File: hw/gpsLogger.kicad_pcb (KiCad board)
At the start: 2 copper layers, 42 x 72.8 mm, 0 parts

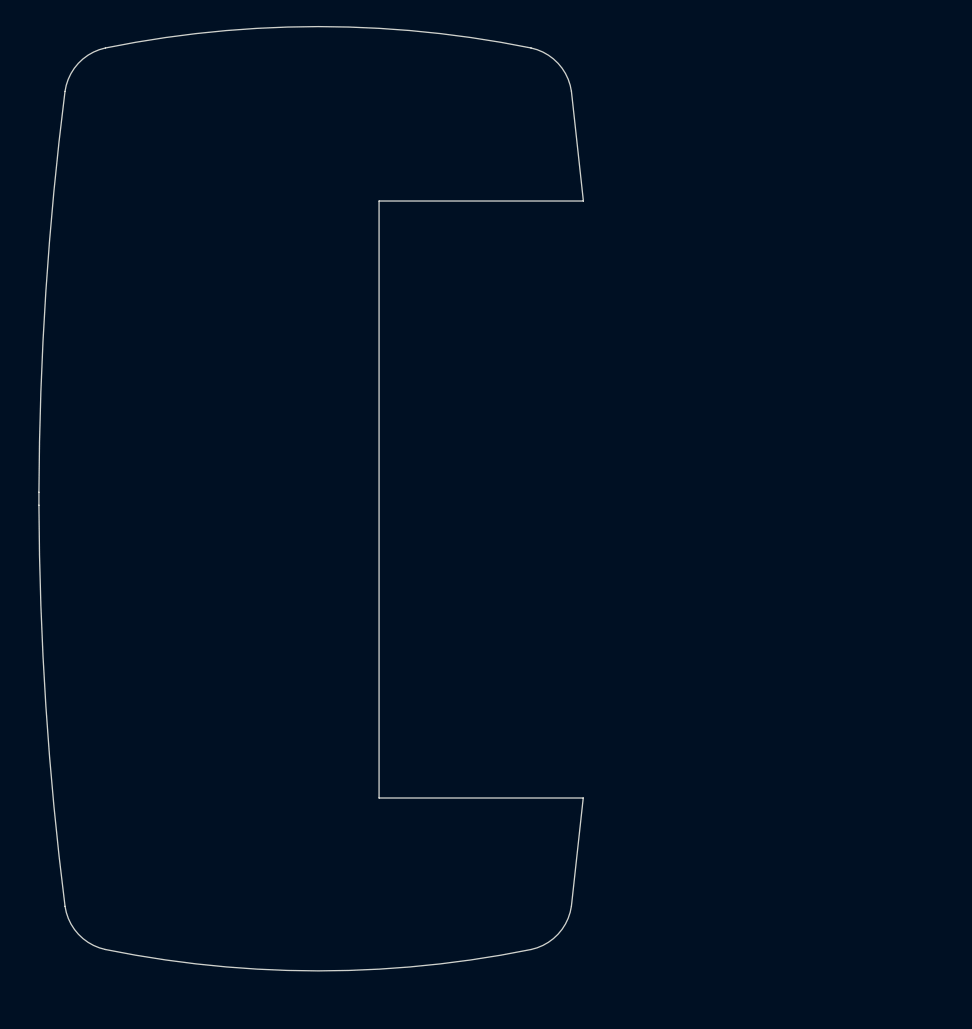
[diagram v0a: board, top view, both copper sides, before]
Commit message: Added USB vertical footprint. uSD card footprint. Did schematic, started rough PCB
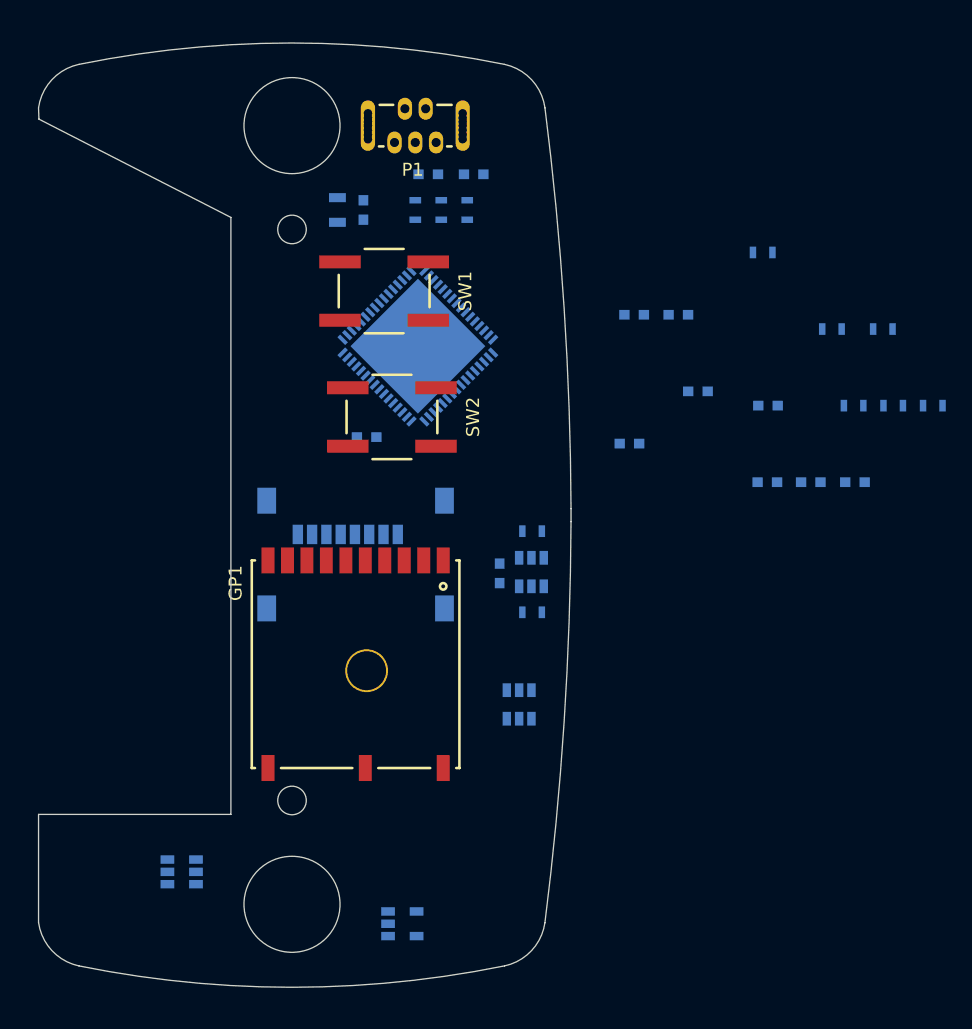
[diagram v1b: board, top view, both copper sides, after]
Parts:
- added C1: C, Capacitors_SMD:C_0603, B.Cu at (147.0, 78.0)
- added C10: C, Capacitors_SMD:C_0603, B.Cu at (172.8, 92.0)
- added C11: C, Capacitors_SMD:C_0603, B.Cu at (178.2, 93.1)
- added C12: C, Capacitors_SMD:C_0603, B.Cu at (171.3, 86.1)
- added C13: C, Capacitors_SMD:C_0603, B.Cu at (184.9, 99.0)
- added C2: C, Capacitors_SMD:C_0603, B.Cu at (155.5, 75.2)
- added C3: C, Capacitors_SMD:C_0603, B.Cu at (152.0, 75.2)
- added C4: C, Capacitors_SMD:C_0603, B.Cu at (147.2, 95.5)
- added C5: C, Capacitors_SMD:C_0603, B.Cu at (157.5, 106.0)
- added C6: C, Capacitors_SMD:C_0603, B.Cu at (178.1, 99.0)
- added C7: C, Capacitors_SMD:C_0603, B.Cu at (167.5, 96.0)
- added C8: C, Capacitors_SMD:C_0603, B.Cu at (167.9, 86.1)
- added C9: C, Capacitors_SMD:C_0603, B.Cu at (181.5, 99.0)
- added FB1: FILTER, Resistors_SMD:R_0805, B.Cu at (145.0, 78.0)
- added GP1: GPS, footprints:PA6C, F.Cu at (147.2, 113.0)
- added IC1: MSP430F55xx, Housings_DFN_QFN:QFN-64-1EP_9x9mm_Pitch0.5mm, B.Cu at (151.2, 88.5)
- added P1: USB_OTG, footprints:USB_VERT, F.Cu at (151.0, 71.5)
- added R1: R, Resistors_SMD:R_0603, B.Cu at (155.0, 78.0)
- added R10: R, Resistors_SMD:R_0603, B.Cu at (177.8, 81.3)
- added R11: 1K, Resistors_SMD:R_0603, B.Cu at (187.0, 87.2)
- added R2: R, Resistors_SMD:R_0603, B.Cu at (153.0, 78.0)
- added R3: R, Resistors_SMD:R_0603, B.Cu at (151.0, 78.0)
- added R4: R, Resistors_SMD:R_0603, B.Cu at (184.8, 93.1)
- added R5: R, Resistors_SMD:R_0603, B.Cu at (160.0, 102.8)
- added R6: R, Resistors_SMD:R_0603, B.Cu at (160.0, 109.0)
- added R7: R, Resistors_SMD:R_0603, B.Cu at (187.8, 93.1)
- added R8: R, Resistors_SMD:R_0603, B.Cu at (190.9, 93.1)
- added R9: 330R, Resistors_SMD:R_0603, B.Cu at (183.1, 87.2)
- added REF**: SolderWirePad_single_2mmDrill, Wire_Pads:SolderWirePad_single_2mmDrill, F.Cu at (141.5, 123.5)
- added REF**: SolderWirePad_single_2mmDrill, Wire_Pads:SolderWirePad_single_2mmDrill, F.Cu at (141.5, 79.5)
- added REF**: SolderWirePad_single_2mmDrill, Wire_Pads:SolderWirePad_single_2mmDrill, F.Cu at (141.5, 131.5)
- added REF**: SolderWirePad_single_2mmDrill, Wire_Pads:SolderWirePad_single_2mmDrill, F.Cu at (141.5, 71.5)
- added SW1: SW_PUSH, cameraTrigger_rev1_0:EVQ_switch, F.Cu at (148.6, 84.2)
- added SW2: SW_PUSH, cameraTrigger_rev1_0:EVQ_switch, F.Cu at (149.2, 94.0)
- added U1: TPS27081A, TO_SOT_Packages_SMD:SOT-23-6, B.Cu at (159.9, 105.9)
- added U2: MCP73812, TO_SOT_Packages_SMD:SOT-23-5, B.Cu at (150.0, 133.0)
- added U3: uSD, footprints:SD_holder_472190001, B.Cu at (145.7, 103.0)
- added U4: TPS27081A, TO_SOT_Packages_SMD:SOT-23-6, B.Cu at (159.0, 116.1)
- added U5: S8261, TO_SOT_Packages_SMD:SOT-23-6, B.Cu at (133.0, 129.0)
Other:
- board size 42 x 72.8 mm -> 41 x 72.8 mm

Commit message: Added LED footprint, and Beagle GPS logo. Schematic done, PCB done.
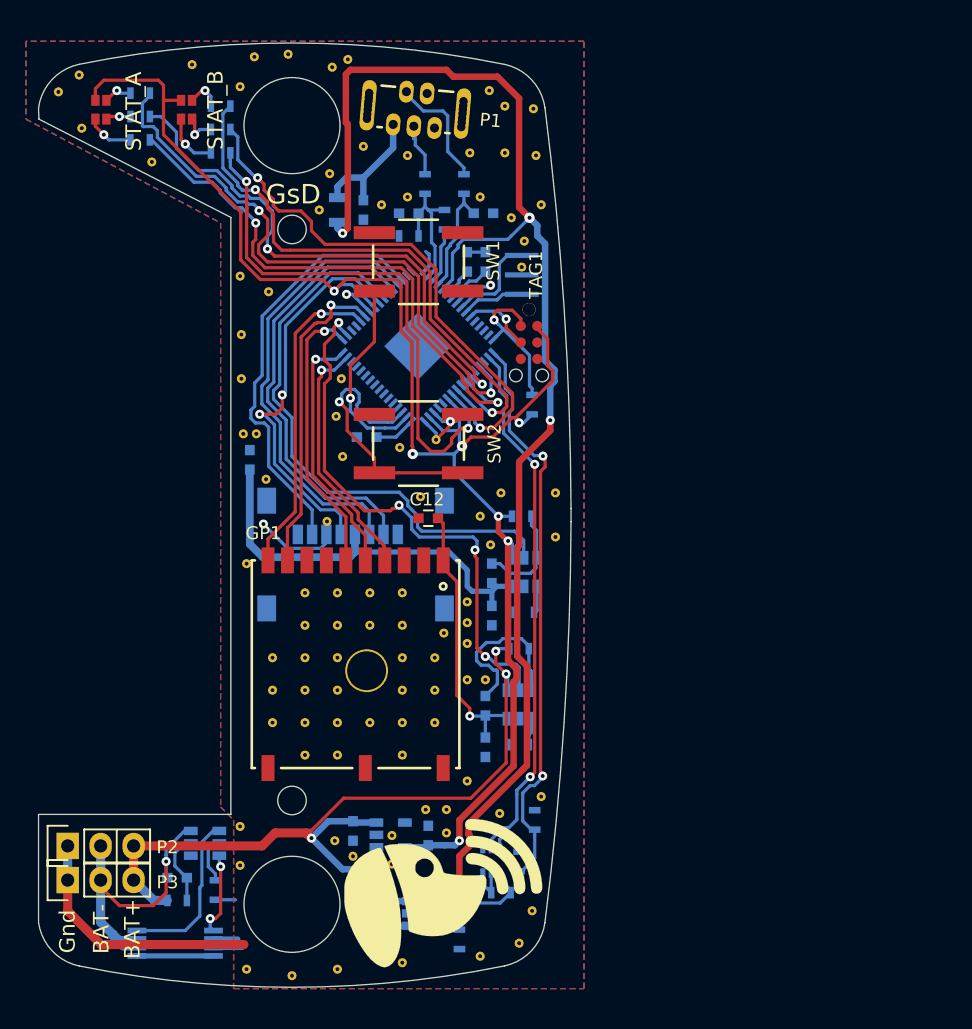
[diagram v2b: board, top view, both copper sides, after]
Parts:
- added C14: C, Capacitors_SMD:C_0603, B.Cu at (146.2, 125.8)
- added C15: C, Capacitors_SMD:C_0603, B.Cu at (152.0, 126.2)
- added C16: C, Capacitors_SMD:C_0603, B.Cu at (156.4, 82.0)
- added C17: C, Capacitors_SMD:C_0603, B.Cu at (155.0, 82.0)
- added D1: Led_RGB_CA, footprints:LITEON_RGB, F.Cu at (126.8, 70.3)
- added D2: Led_RGB_CA, footprints:LITEON_RGB, F.Cu at (133.4, 70.3)
- added G***: LOGO, LOGO, F.Cu at (152.8, 130.8)
- added P2: CONN_01X03, Socket_Strips:Socket_Strip_Straight_1x03, F.Cu at (124.2, 127.0)
- added P3: CONN_01X03, Socket_Strips:Socket_Strip_Straight_1x03, F.Cu at (124.2, 129.6)
- added Q1: Q_NMOS_AO8810, Housings_SSOP:TSSOP-8_4.4x3mm_Pitch0.65mm, B.Cu at (132.5, 134.5)
- added Q2: FG6943010R, TO_SOT_Packages_SMD:SC-70-6, B.Cu at (156.9, 128.1)
- added R12: R, Resistors_SMD:R_0603, B.Cu at (157.6, 130.6)
- added R13: R, Resistors_SMD:R_0603, B.Cu at (159.0, 128.2)
- added R14: R, Resistors_SMD:R_0603, B.Cu at (160.2, 125.0)
- added R15: R, Resistors_SMD:R_0603, B.Cu at (160.0, 93.0)
- added R16: R, Resistors_SMD:R_0603, B.Cu at (129.8, 69.0)
- added R17: R, Resistors_SMD:R_0603, B.Cu at (129.8, 70.8)
- added R18: R, Resistors_SMD:R_0603, B.Cu at (129.8, 72.6)
- added R19: R, Resistors_SMD:R_0603, B.Cu at (136.0, 70.0)
- added R20: R, Resistors_SMD:R_0603, B.Cu at (136.0, 71.8)
- added R21: R, Resistors_SMD:R_0603, B.Cu at (136.0, 73.6)
- added REF**: SolderWirePad_single_2mmDrill, Wire_Pads:SolderWirePad_single_2mmDrill, F.Cu at (160.7, 123.2)
- added REF**: SolderWirePad_single_2mmDrill, Wire_Pads:SolderWirePad_single_2mmDrill, F.Cu at (160.7, 77.6)
- added REF**: SolderWirePad_single_2mmDrill, Wire_Pads:SolderWirePad_single_2mmDrill, F.Cu at (160.1, 70.2)
- added REF**: SolderWirePad_single_2mmDrill, Wire_Pads:SolderWirePad_single_2mmDrill, F.Cu at (160.3, 73.8)
- added REF**: SolderWirePad_single_2mmDrill, Wire_Pads:SolderWirePad_single_2mmDrill, F.Cu at (157.9, 73.6)
- added REF**: SolderWirePad_single_2mmDrill, Wire_Pads:SolderWirePad_single_2mmDrill, F.Cu at (157.9, 70.0)
- added REF**: SolderWirePad_single_2mmDrill, Wire_Pads:SolderWirePad_single_2mmDrill, F.Cu at (156.7, 68.8)
- added REF**: SolderWirePad_single_2mmDrill, Wire_Pads:SolderWirePad_single_2mmDrill, F.Cu at (137.6, 87.6)
- added REF**: SolderWirePad_single_2mmDrill, Wire_Pads:SolderWirePad_single_2mmDrill, F.Cu at (137.6, 91.0)
- added REF**: SolderWirePad_single_2mmDrill, Wire_Pads:SolderWirePad_single_2mmDrill, F.Cu at (137.5, 83.1)
- added REF**: SolderWirePad_single_2mmDrill, Wire_Pads:SolderWirePad_single_2mmDrill, F.Cu at (139.7, 84.3)
- added REF**: SolderWirePad_single_2mmDrill, Wire_Pads:SolderWirePad_single_2mmDrill, F.Cu at (137.5, 68.5)
- added REF**: SolderWirePad_single_2mmDrill, Wire_Pads:SolderWirePad_single_2mmDrill, F.Cu at (145.3, 91.0)
- added REF**: SolderWirePad_single_2mmDrill, Wire_Pads:SolderWirePad_single_2mmDrill, F.Cu at (144.9, 93.9)
- added REF**: SolderWirePad_single_2mmDrill, Wire_Pads:SolderWirePad_single_2mmDrill, F.Cu at (145.4, 97.0)
- added REF**: SolderWirePad_single_2mmDrill, Wire_Pads:SolderWirePad_single_2mmDrill, F.Cu at (149.8, 96.3)
- added REF**: SolderWirePad_single_2mmDrill, Wire_Pads:SolderWirePad_single_2mmDrill, F.Cu at (152.6, 95.7)
- added REF**: SolderWirePad_single_2mmDrill, Wire_Pads:SolderWirePad_single_2mmDrill, F.Cu at (157.5, 124.5)
- added REF**: SolderWirePad_single_2mmDrill, Wire_Pads:SolderWirePad_single_2mmDrill, F.Cu at (155.0, 122.0)
- added REF**: SolderWirePad_single_2mmDrill, Wire_Pads:SolderWirePad_single_2mmDrill, F.Cu at (137.5, 125.5)
- added REF**: SolderWirePad_single_2mmDrill, Wire_Pads:SolderWirePad_single_2mmDrill, F.Cu at (137.5, 128.5)
- added REF**: SolderWirePad_single_2mmDrill, Wire_Pads:SolderWirePad_single_2mmDrill, F.Cu at (160.0, 132.0)
- added REF**: SolderWirePad_single_2mmDrill, Wire_Pads:SolderWirePad_single_2mmDrill, F.Cu at (130.7, 74.3)
- added REF**: SolderWirePad_single_2mmDrill, Wire_Pads:SolderWirePad_single_2mmDrill, F.Cu at (159.0, 134.5)
- added REF**: SolderWirePad_single_2mmDrill, Wire_Pads:SolderWirePad_single_2mmDrill, F.Cu at (156.0, 135.5)
- added REF**: SolderWirePad_single_2mmDrill, Wire_Pads:SolderWirePad_single_2mmDrill, F.Cu at (150.0, 136.0)
- added REF**: SolderWirePad_single_2mmDrill, Wire_Pads:SolderWirePad_single_2mmDrill, F.Cu at (145.0, 136.5)
- added REF**: SolderWirePad_single_2mmDrill, Wire_Pads:SolderWirePad_single_2mmDrill, F.Cu at (141.5, 137.0)
- added REF**: SolderWirePad_single_2mmDrill, Wire_Pads:SolderWirePad_single_2mmDrill, F.Cu at (138.0, 136.5)
- added REF**: SolderWirePad_single_2mmDrill, Wire_Pads:SolderWirePad_single_2mmDrill, F.Cu at (150.0, 107.5)
- added REF**: SolderWirePad_single_2mmDrill, Wire_Pads:SolderWirePad_single_2mmDrill, F.Cu at (152.5, 115.0)
- added REF**: SolderWirePad_single_2mmDrill, Wire_Pads:SolderWirePad_single_2mmDrill, F.Cu at (152.5, 112.5)
- added REF**: SolderWirePad_single_2mmDrill, Wire_Pads:SolderWirePad_single_2mmDrill, F.Cu at (145.0, 112.5)
- added REF**: SolderWirePad_single_2mmDrill, Wire_Pads:SolderWirePad_single_2mmDrill, F.Cu at (125.3, 71.7)
- added REF**: SolderWirePad_single_2mmDrill, Wire_Pads:SolderWirePad_single_2mmDrill, F.Cu at (142.5, 112.5)
- added REF**: SolderWirePad_single_2mmDrill, Wire_Pads:SolderWirePad_single_2mmDrill, F.Cu at (140.0, 112.5)
- added REF**: SolderWirePad_single_2mmDrill, Wire_Pads:SolderWirePad_single_2mmDrill, F.Cu at (142.5, 110.0)
- added REF**: SolderWirePad_single_2mmDrill, Wire_Pads:SolderWirePad_single_2mmDrill, F.Cu at (145.0, 110.0)
- added REF**: SolderWirePad_single_2mmDrill, Wire_Pads:SolderWirePad_single_2mmDrill, F.Cu at (147.5, 110.0)
- added REF**: SolderWirePad_single_2mmDrill, Wire_Pads:SolderWirePad_single_2mmDrill, F.Cu at (150.0, 110.0)
- added REF**: SolderWirePad_single_2mmDrill, Wire_Pads:SolderWirePad_single_2mmDrill, F.Cu at (150.0, 112.5)
- added REF**: SolderWirePad_single_2mmDrill, Wire_Pads:SolderWirePad_single_2mmDrill, F.Cu at (150.0, 115.0)
- added REF**: SolderWirePad_single_2mmDrill, Wire_Pads:SolderWirePad_single_2mmDrill, F.Cu at (145.0, 115.0)
- added REF**: SolderWirePad_single_2mmDrill, Wire_Pads:SolderWirePad_single_2mmDrill, F.Cu at (142.5, 115.0)
- added REF**: SolderWirePad_single_2mmDrill, Wire_Pads:SolderWirePad_single_2mmDrill, F.Cu at (123.5, 68.9)
- added REF**: SolderWirePad_single_2mmDrill, Wire_Pads:SolderWirePad_single_2mmDrill, F.Cu at (152.5, 117.5)
- added REF**: SolderWirePad_single_2mmDrill, Wire_Pads:SolderWirePad_single_2mmDrill, F.Cu at (150.0, 117.5)
- added REF**: SolderWirePad_single_2mmDrill, Wire_Pads:SolderWirePad_single_2mmDrill, F.Cu at (147.5, 117.5)
- added REF**: SolderWirePad_single_2mmDrill, Wire_Pads:SolderWirePad_single_2mmDrill, F.Cu at (145.0, 117.5)
- added REF**: SolderWirePad_single_2mmDrill, Wire_Pads:SolderWirePad_single_2mmDrill, F.Cu at (142.5, 117.5)
- added REF**: SolderWirePad_single_2mmDrill, Wire_Pads:SolderWirePad_single_2mmDrill, F.Cu at (145.0, 120.0)
- added REF**: SolderWirePad_single_2mmDrill, Wire_Pads:SolderWirePad_single_2mmDrill, F.Cu at (142.5, 120.0)
- added REF**: SolderWirePad_single_2mmDrill, Wire_Pads:SolderWirePad_single_2mmDrill, F.Cu at (138.6, 66.2)
- added REF**: SolderWirePad_single_2mmDrill, Wire_Pads:SolderWirePad_single_2mmDrill, F.Cu at (141.2, 66.0)
- added REF**: SolderWirePad_single_2mmDrill, Wire_Pads:SolderWirePad_single_2mmDrill, F.Cu at (145.8, 66.4)
- added REF**: SolderWirePad_single_2mmDrill, Wire_Pads:SolderWirePad_single_2mmDrill, F.Cu at (125.1, 67.6)
- added REF**: SolderWirePad_single_2mmDrill, Wire_Pads:SolderWirePad_single_2mmDrill, F.Cu at (144.6, 67.0)
- added REF**: SolderWirePad_single_2mmDrill, Wire_Pads:SolderWirePad_single_2mmDrill, F.Cu at (144.4, 75.2)
- added REF**: SolderWirePad_single_2mmDrill, Wire_Pads:SolderWirePad_single_2mmDrill, F.Cu at (143.6, 78.0)
- added REF**: SolderWirePad_single_2mmDrill, Wire_Pads:SolderWirePad_single_2mmDrill, F.Cu at (155.2, 73.6)
- added REF**: SolderWirePad_single_2mmDrill, Wire_Pads:SolderWirePad_single_2mmDrill, F.Cu at (150.4, 73.8)
- added REF**: SolderWirePad_single_2mmDrill, Wire_Pads:SolderWirePad_single_2mmDrill, F.Cu at (150.4, 77.0)
- added REF**: SolderWirePad_single_2mmDrill, Wire_Pads:SolderWirePad_single_2mmDrill, F.Cu at (156.0, 77.0)
- added REF**: SolderWirePad_single_2mmDrill, Wire_Pads:SolderWirePad_single_2mmDrill, F.Cu at (158.4, 78.6)
- added REF**: SolderWirePad_single_2mmDrill, Wire_Pads:SolderWirePad_single_2mmDrill, F.Cu at (159.2, 82.4)
- added REF**: SolderWirePad_single_2mmDrill, Wire_Pads:SolderWirePad_single_2mmDrill, F.Cu at (159.4, 80.4)
- added REF**: SolderWirePad_single_2mmDrill, Wire_Pads:SolderWirePad_single_2mmDrill, F.Cu at (133.8, 66.8)
- added REF**: SolderWirePad_single_2mmDrill, Wire_Pads:SolderWirePad_single_2mmDrill, F.Cu at (156.0, 101.6)
- added REF**: SolderWirePad_single_2mmDrill, Wire_Pads:SolderWirePad_single_2mmDrill, F.Cu at (157.6, 99.8)
- added REF**: SolderWirePad_single_2mmDrill, Wire_Pads:SolderWirePad_single_2mmDrill, F.Cu at (161.8, 103.2)
- added REF**: SolderWirePad_single_2mmDrill, Wire_Pads:SolderWirePad_single_2mmDrill, F.Cu at (161.8, 99.8)
- added REF**: SolderWirePad_single_2mmDrill, Wire_Pads:SolderWirePad_single_2mmDrill, F.Cu at (156.8, 103.8)
- added REF**: SolderWirePad_single_2mmDrill, Wire_Pads:SolderWirePad_single_2mmDrill, F.Cu at (150.0, 120.0)
- added REF**: SolderWirePad_single_2mmDrill, Wire_Pads:SolderWirePad_single_2mmDrill, F.Cu at (153.2, 110.6)
- added REF**: SolderWirePad_single_2mmDrill, Wire_Pads:SolderWirePad_single_2mmDrill, F.Cu at (155.0, 114.2)
- added REF**: SolderWirePad_single_2mmDrill, Wire_Pads:SolderWirePad_single_2mmDrill, F.Cu at (156.4, 114.2)
- added REF**: SolderWirePad_single_2mmDrill, Wire_Pads:SolderWirePad_single_2mmDrill, F.Cu at (155.0, 111.4)
- added REF**: SolderWirePad_single_2mmDrill, Wire_Pads:SolderWirePad_single_2mmDrill, F.Cu at (148.4, 77.6)
- added REF**: SolderWirePad_single_2mmDrill, Wire_Pads:SolderWirePad_single_2mmDrill, F.Cu at (155.0, 109.8)
- added REF**: SolderWirePad_single_2mmDrill, Wire_Pads:SolderWirePad_single_2mmDrill, F.Cu at (155.0, 108.2)
- added REF**: SolderWirePad_single_2mmDrill, Wire_Pads:SolderWirePad_single_2mmDrill, F.Cu at (153.4, 124.2)
- added REF**: SolderWirePad_single_2mmDrill, Wire_Pads:SolderWirePad_single_2mmDrill, F.Cu at (153.4, 126.0)
- added REF**: SolderWirePad_single_2mmDrill, Wire_Pads:SolderWirePad_single_2mmDrill, F.Cu at (151.8, 124.2)
- added REF**: SolderWirePad_single_2mmDrill, Wire_Pads:SolderWirePad_single_2mmDrill, F.Cu at (149.2, 128.4)
- added REF**: SolderWirePad_single_2mmDrill, Wire_Pads:SolderWirePad_single_2mmDrill, F.Cu at (149.2, 126.2)
- added REF**: SolderWirePad_single_2mmDrill, Wire_Pads:SolderWirePad_single_2mmDrill, F.Cu at (146.2, 127.8)
- added REF**: SolderWirePad_single_2mmDrill, Wire_Pads:SolderWirePad_single_2mmDrill, F.Cu at (144.8, 126.6)
- added REF**: SolderWirePad_single_2mmDrill, Wire_Pads:SolderWirePad_single_2mmDrill, F.Cu at (147.5, 107.5)
- added REF**: SolderWirePad_single_2mmDrill, Wire_Pads:SolderWirePad_single_2mmDrill, F.Cu at (147.0, 73.1)
- added REF**: SolderWirePad_single_2mmDrill, Wire_Pads:SolderWirePad_single_2mmDrill, F.Cu at (142.5, 107.5)
- added REF**: SolderWirePad_single_2mmDrill, Wire_Pads:SolderWirePad_single_2mmDrill, F.Cu at (145.0, 107.5)
- added REF**: SolderWirePad_single_2mmDrill, Wire_Pads:SolderWirePad_single_2mmDrill, F.Cu at (138.0, 105.2)
- added REF**: SolderWirePad_single_2mmDrill, Wire_Pads:SolderWirePad_single_2mmDrill, F.Cu at (137.8, 95.2)
- added REF**: SolderWirePad_single_2mmDrill, Wire_Pads:SolderWirePad_single_2mmDrill, F.Cu at (138.8, 95.2)
- added REF**: SolderWirePad_single_2mmDrill, Wire_Pads:SolderWirePad_single_2mmDrill, F.Cu at (139.5, 98.8)
- added REF**: SolderWirePad_single_2mmDrill, Wire_Pads:SolderWirePad_single_2mmDrill, F.Cu at (151.4, 100.1)
- added REF**: SolderWirePad_single_2mmDrill, Wire_Pads:SolderWirePad_single_2mmDrill, F.Cu at (144.2, 102.0)
- added REF**: SolderWirePad_single_2mmDrill, Wire_Pads:SolderWirePad_single_2mmDrill, F.Cu at (140.0, 115.0)
- added REF**: SolderWirePad_single_2mmDrill, Wire_Pads:SolderWirePad_single_2mmDrill, F.Cu at (140.0, 117.5)
- added TAG1: TAG_CONNECT, lib:tag_connect, F.Cu at (159.8, 88.2)
- added U6: TPS78230, TO_SOT_Packages_SMD:SOT-23-5, B.Cu at (149.1, 126.2)
- added X1: CRYSTAL_SMD, lib:CSTCR_G15C, B.Cu at (159.2, 83.0)
- C12: moved to F.Cu
- moved R11 67.2 mm to (135.6, 130.4), turned to 270 degrees
- moved R9 67.0 mm to (132.7, 131.2), turned to 180 degrees
- moved C11 58.3 mm to (132.7, 129.4), turned to 180 degrees
- moved R7 53.0 mm to (154.4, 134.2), turned to 90 degrees
- moved C9 46.5 mm to (147.8, 131.0), turned to 180 degrees
- moved C6 46.0 mm to (148.8, 134.4), turned to 270 degrees
- moved R10 42.3 mm to (159.0, 119.2), turned to 180 degrees
- moved R8 37.0 mm to (159.0, 111.8), turned to 180 degrees
- moved C13 35.0 mm to (156.4, 119.4), turned to 270 degrees
- moved R4 34.6 mm to (153.2, 78.8), turned to 90 degrees
- moved C7 29.3 mm to (138.2, 97.2), turned to 90 degrees
- moved C10 29.2 mm to (156.4, 116.2), turned to 90 degrees
- moved C8 25.6 mm to (156.9, 109.2), turned to 270 degrees
- moved C12 24.8 mm to (152.0, 101.8), turned to 180 degrees
- moved SW1 3.48 mm to (151.2, 82.0)
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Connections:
- C2 pad 1: /D- -> /DM
- C3 pad 1: /D+ -> /DP
- GP1 pad 4: Net-(GP1-Pad4) -> /GPS_BACKUP
- IC1 pad 1: Net-(IC1-Pad1) -> /V_SENSE
- IC1 pad 10: Net-(IC1-Pad10) -> /LED_B_B
- IC1 pad 18: Net-(IC1-Pad18) -> /PWR_BUT
- IC1 pad 19: Net-(IC1-Pad19) -> /NEW_BUT
- IC1 pad 2: Net-(IC1-Pad2) -> /SENSE_EN
- IC1 pad 31: Net-(IC1-Pad31) -> /GPS_BACKUP
- IC1 pad 32: Net-(IC1-Pad32) -> /GPS_FIX
- IC1 pad 33: Net-(IC1-Pad33) -> /GPS_PPS
- IC1 pad 34: Net-(IC1-Pad34) -> /GPS_PWR
- IC1 pad 37: Net-(IC1-Pad37) -> /GPS_MOSI
- IC1 pad 38: Net-(IC1-Pad38) -> /GPS_MISO
- IC1 pad 4: Net-(IC1-Pad4) -> /LED_A_R
- IC1 pad 41: Net-(IC1-Pad41) -> /SD_CLK
- IC1 pad 42: Net-(IC1-Pad42) -> /SD_PWR
- IC1 pad 44: Net-(IC1-Pad44) -> /SD_CS
- IC1 pad 45: Net-(IC1-Pad45) -> /SD_MOSI
- IC1 pad 46: Net-(IC1-Pad46) -> /SD_MISO
- IC1 pad 52: Net-(IC1-Pad52) -> /DM
- IC1 pad 57: Net-(IC1-Pad57) -> /OSC_OUT
- IC1 pad 58: Net-(IC1-Pad58) -> /OSC_IN
- IC1 pad 59: Net-(IC1-Pad59) -> /TEST
- IC1 pad 6: Net-(IC1-Pad6) -> /LED_A_G
- IC1 pad 64: Net-(IC1-Pad64) -> /RST
- IC1 pad 7: Net-(IC1-Pad7) -> /LED_A_B
- IC1 pad 8: Net-(IC1-Pad8) -> /LED_B_R
- IC1 pad 9: Net-(IC1-Pad9) -> /LED_B_G
- R3 pad 2: /D+ -> /DP
- R4 pad 2: /D+ -> /DP
- R8 pad 2: +3V3 -> +BATT
- U3 pad 3: /MOSI -> /SD_MOSI
- U3 pad 5: /SCLK -> /SD_CLK
- U3 pad 7: /MISO -> /SD_MISO
- U4 pad 4: +3V3 -> +BATT
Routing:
- net +3V3: track 0.00 -> 122.4 mm, vias 0 -> 7
- net VBUS: track 0.00 -> 111.8 mm, vias 0 -> 4
- net +BATT: track 0.00 -> 77.6 mm, vias 0 -> 3
- net GND: track 0.00 -> 48.0 mm, vias 0 -> 4
- net /LED_A_R: track 0.00 -> 46.1 mm, vias 0 -> 2
- net /V_SENSE: track 0.00 -> 44.4 mm, vias 0 -> 2
- net /SD_PWR: track 0.00 -> 44.1 mm
- net /LED_B_R: track 0.00 -> 43.4 mm, vias 0 -> 2
- net /LED_B_B: track 0.00 -> 43.1 mm, vias 0 -> 2
- net /LED_A_B: track 0.00 -> 42.9 mm, vias 0 -> 2
- net /GPS_PWR: track 0.00 -> 42.4 mm, vias 0 -> 4
- net /LED_B_G: track 0.00 -> 42.3 mm, vias 0 -> 2
- net /SENSE_EN: track 0.00 -> 41.2 mm, vias 0 -> 2
- net /LED_A_G: track 0.00 -> 40.8 mm, vias 0 -> 2
- net /SD_MOSI: track 0.00 -> 34.6 mm
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- added copper zone on B.Cu, net GND
- added copper zone on F.Cu, net GND
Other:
- net class Default: via_dia 0.6 -> 0.7; via_drill 0.4 -> 0.3
- net class Power added: clearance 0.2, trace_width 0.25, via_dia 0.7, via_drill 0.3
- rule trace_min: 0.2 -> 0.18
- rule via_min_size: 0.4 -> 0.7
- board text added: "BAT+"
- board text added: "BAT-"
- board text added: "Gnd"
- board text added: "GsD"
- board text added: "STAT_A"
- board text added: "STAT_B"

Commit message: Created Gerbers
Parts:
- added G***: LOGO, LOGO, F.Cu at (148.8, 75.8)
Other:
- board text added: "github.com/Greeeg/gpsLogger"

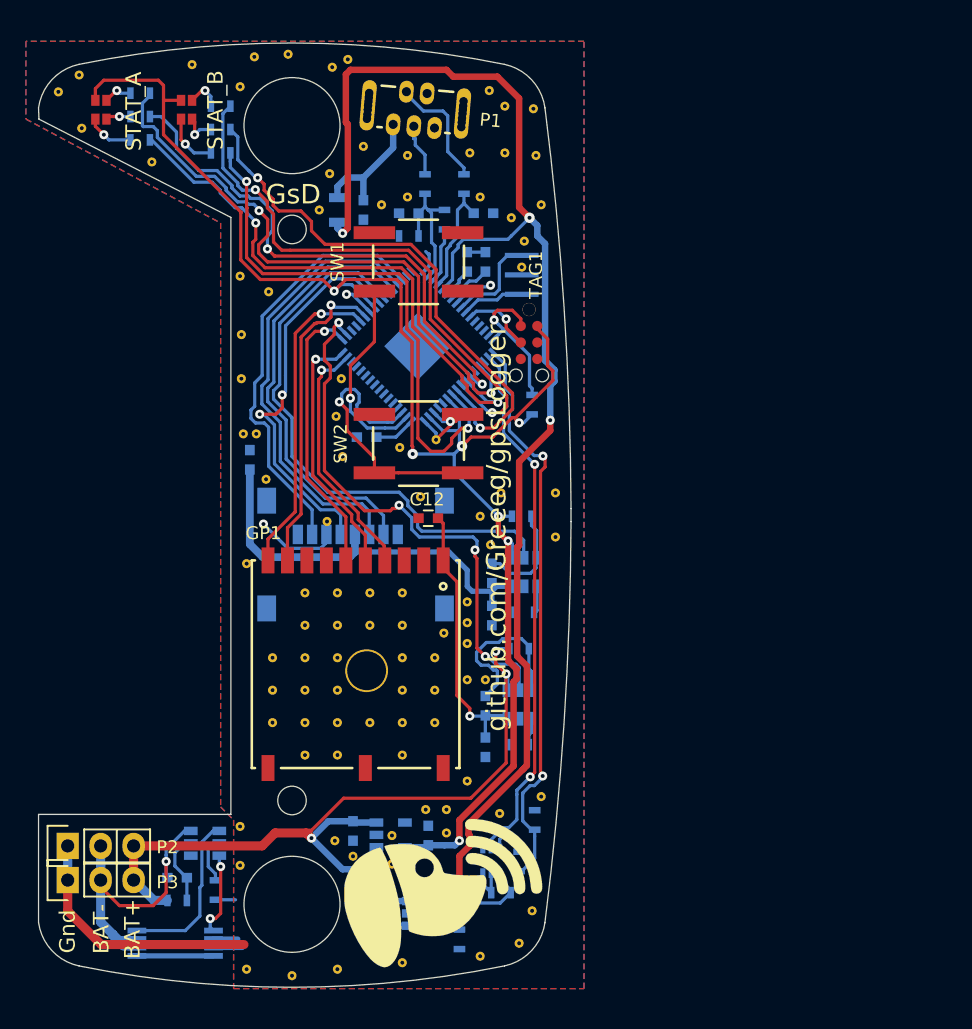
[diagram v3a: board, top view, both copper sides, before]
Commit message: add footprint for MAX M8Q GPS, Unroute PCB, Adjust schematic
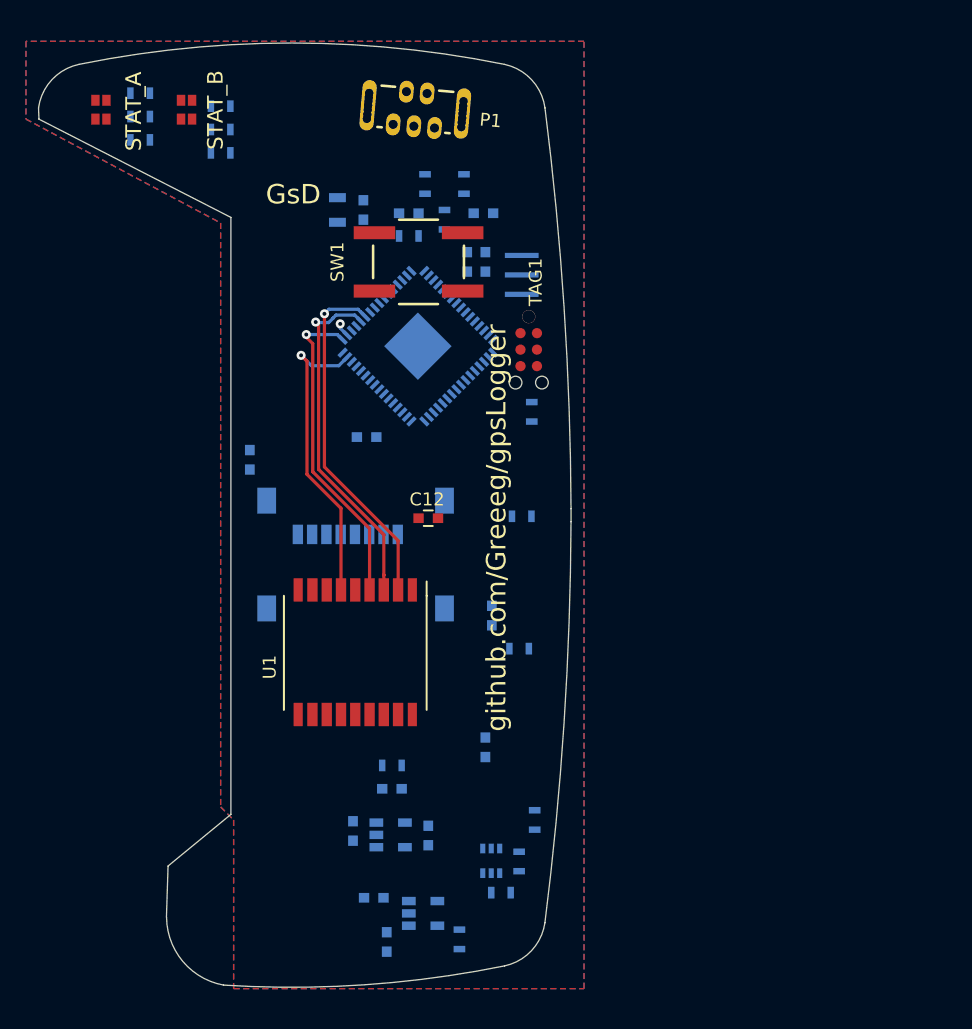
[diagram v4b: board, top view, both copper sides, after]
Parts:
- removed C10, C11: C, Capacitors_SMD:C_0603
- removed G*** (x2): LOGO, LOGO
- removed GP1: GPS, footprints:PA6C
- removed P2, P3: CONN_01X03, Socket_Strips:Socket_Strip_Straight_1x03
- removed Q1: Q_NMOS_AO8810, Housings_SSOP:TSSOP-8_4.4x3mm_Pitch0.65mm
- removed R10: R, Resistors_SMD:R_0603
- removed R11: 1K, Resistors_SMD:R_0603
- removed R9: 330R, Resistors_SMD:R_0603
- removed REF** (x103): SolderWirePad_single_2mmDrill, Wire_Pads:SolderWirePad_single_2mmDrill
- removed SW2: SW_PUSH, cameraTrigger_rev1_0:EVQ_switch
- removed U4: TPS27081A, TO_SOT_Packages_SMD:SOT-23-6
- removed U5: S8261, TO_SOT_Packages_SMD:SOT-23-6
- C12: value C -> 100n
- C13: value C -> 1u
- C5: value C -> 10n
- R5, R8: value R -> 10k
- R6: value R -> 10R
- U1: value TPS27081A -> MAX_M8Q; footprint TO_SOT_Packages_SMD:SOT-23-6 -> footprints:MAX_M8; moved to F.Cu
- moved C5 18.3 mm to (149.2, 122.6), turned to 0 degrees
- moved R6 15.6 mm to (149.2, 120.8)
- moved U1 14.4 mm to (146.4, 112.1)
- moved TAG1 0.55 mm to (159.7, 88.8)
- moved R15 0.55 mm to (160.0, 93.5)
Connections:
- C12 pad 1: /GPS_VCC -> GPS_VCC
- C13 pad 1: /GPS_VCC -> GPS_VCC
- C5 pad 1: /SD_VCC -> Net-(C5-Pad1)
- C5 pad 2: Net-(C5-Pad2) -> GND
- IC1 pad 31: /GPS_BACKUP -> GPS_BACKUP
- IC1 pad 33: /GPS_PPS -> GPS_PPS
- IC1 pad 37: /GPS_MOSI -> GPS_MOSI
- IC1 pad 38: /GPS_MISO -> GPS_MISO
- R5 pad 1: Net-(C5-Pad2) -> Net-(R5-Pad1)
- R5 pad 2: +3V3 -> GPS_VCC
- R6 pad 1: Net-(R6-Pad1) -> GPS_VCC_RF
- R6 pad 2: GND -> Net-(C5-Pad1)
- R8 pad 1: Net-(C10-Pad2) -> GPS_VCC
- R8 pad 2: +BATT -> Net-(R8-Pad2)
- U1 pad 1: Net-(R6-Pad1) -> GND
- U1 pad 2: /SD_VCC -> GPS_MISO
- U1 pad 3: /SD_VCC -> GPS_MOSI
- U1 pad 4: +3V3 -> GPS_PPS
- U1 pad 5: /SD_PWR -> Net-(U1-Pad5)
- U1 pad 6: Net-(C5-Pad2) -> GPS_BACKUP
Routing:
- net +3V3: track 122.4 -> 0.00 mm, vias 7 -> 0
- net VBUS: track 111.8 -> 0.00 mm, vias 4 -> 0
- net +BATT: track 77.6 -> 0.00 mm, vias 3 -> 0
- net GND: track 48.0 -> 0.00 mm, vias 4 -> 0
- net /LED_A_R: track 46.1 -> 0.00 mm, vias 2 -> 0
- net /V_SENSE: track 44.4 -> 0.00 mm, vias 2 -> 0
- net /SD_PWR: track 44.1 -> 0.00 mm
- net /LED_B_R: track 43.4 -> 0.00 mm, vias 2 -> 0
- net /LED_B_B: track 43.1 -> 0.00 mm, vias 2 -> 0
- net /LED_A_B: track 42.9 -> 0.00 mm, vias 2 -> 0
- net /LED_B_G: track 42.3 -> 0.00 mm, vias 2 -> 0
- net /GPS_PWR: track 42.4 -> 1.10 mm, vias 4 -> 1
- net /SENSE_EN: track 41.2 -> 0.00 mm, vias 2 -> 0
- net /LED_A_G: track 40.8 -> 0.00 mm, vias 2 -> 0
- net /SD_MOSI: track 34.6 -> 0.00 mm
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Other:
- outline, holes or cut-outs redrawn
- board text removed: "BAT+"
- board text removed: "BAT-"
- board text removed: "Gnd"
